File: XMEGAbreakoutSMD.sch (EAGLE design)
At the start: 22 parts, among them IC1 XMEGA16A4A

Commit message: smd breakout finished
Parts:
- added JUMPER1, JUMPER2: 0, fab:RES-US1206FAB
- IC1: value XMEGA16A4A -> XMEGA16A4; device atmel:XMEGA16A4A -> atmel:XMEGA16A4
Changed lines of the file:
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@@
 </classes>
 <parts>
-<part name="IC1" library="atmel" deviceset="XMEGA16A4" device="A"/>
+<part name="IC1" library="atmel" deviceset="XMEGA16A4" device="" value="XMEGA16A4"/>
 <part name="JP2" library="SparkFun" deviceset="M08" device="SMD-STRAIGHT-ALT"/>
 <part name="JP3" library="SparkFun" deviceset="M08" device="SMD-STRAIGHT-ALT"/>
@@
 <part name="D4" library="fab" deviceset="ZENER_DIODE" device="SOD123"/>
 <part name="D5" library="fab" deviceset="ZENER_DIODE" device="SOD123"/>
+<part name="JUMPER1" library="fab" deviceset="RES-US" device="1206FAB" value="0"/>
+<part name="JUMPER2" library="fab" deviceset="RES-US" device="1206FAB" value="0"/>
 </parts>
 <sheets>
@@
 <instance part="D4" gate="1" x="-50.8" y="124.46" rot="R90"/>
 <instance part="D5" gate="1" x="-30.48" y="124.46" rot="R90"/>
+<instance part="JUMPER1" gate="G$1" x="0" y="175.26"/>
+<instance part="JUMPER2" gate="G$1" x="0" y="167.64"/>
 </instances>
 <busses>
@@
 <net name="D+" class="0">
 <segment>
-<pinref part="U$1" gate="G$1" pin="D+"/>
-<wire x1="-60.96" y1="152.4" x2="-55.88" y2="152.4" width="0.1524" layer="91"/>
-<wire x1="-55.88" y1="152.4" x2="-55.88" y2="129.54" width="0.1524" layer="91"/>
-<wire x1="-55.88" y1="129.54" x2="-38.1" y2="129.54" width="0.1524" layer="91"/>
-<label x="-17.78" y="129.54" size="1.778" layer="95"/>
-<pinref part="D2" gate="1" pin="ANODE"/>
-<wire x1="-38.1" y1="129.54" x2="-15.24" y2="129.54" width="0.1524" layer="91"/>
-<wire x1="-38.1" y1="132.08" x2="-38.1" y2="129.54" width="0.1524" layer="91"/>
-<junction x="-38.1" y="129.54"/>
-<pinref part="D3" gate="1" pin="CATHODE"/>
-<wire x1="-38.1" y1="127" x2="-38.1" y2="129.54" width="0.1524" layer="91"/>
-</segment>
-<segment>
 <pinref part="IC1" gate="G$1" pin="PD6"/>
 <pinref part="JP3" gate="G$1" pin="2"/>
@@
 <label x="76.2" y="22.86" size="1.778" layer="95"/>
 </segment>
-</net>
+<segment>
+<pinref part="U$1" gate="G$1" pin="D+"/>
+<wire x1="-60.96" y1="152.4" x2="-55.88" y2="152.4" width="0.1524" layer="91"/>
+<wire x1="-55.88" y1="152.4" x2="-55.88" y2="129.54" width="0.1524" layer="91"/>
+<wire x1="-55.88" y1="129.54" x2="-48.26" y2="129.54" width="0.1524" layer="91"/>
+<wire x1="-38.1" y1="129.54" x2="-15.24" y2="129.54" width="0.1524" layer="91"/>
+<label x="-20.32" y="129.54" size="1.778" layer="95"/>
+<pinref part="D3" gate="1" pin="CATHODE"/>
+<wire x1="-38.1" y1="127" x2="-38.1" y2="129.54" width="0.1524" layer="91"/>
+<junction x="-38.1" y="129.54"/>
+<pinref part="D2" gate="1" pin="ANODE"/>
+<wire x1="-38.1" y1="129.54" x2="-38.1" y2="132.08" width="0.1524" layer="91"/>
+<wire x1="-48.26" y1="129.54" x2="-38.1" y2="129.54" width="0.1524" layer="91"/>
+</segment>
+</net>

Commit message: small changes
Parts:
- added C5: 4.7uF, fab:CAP-US1206
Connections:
- net GND: now also C5.2
- net VBUS: now also C5.1
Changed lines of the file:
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@@
 <part name="JUMPER1" library="fab" deviceset="RES-US" device="1206FAB" value="0"/>
 <part name="JUMPER2" library="fab" deviceset="RES-US" device="1206FAB" value="0"/>
+<part name="C5" library="fab" deviceset="CAP-US" device="1206" value="4.7uF"/>
 </parts>
 <sheets>
@@
 <instance part="JUMPER1" gate="G$1" x="0" y="175.26"/>
 <instance part="JUMPER2" gate="G$1" x="0" y="167.64"/>
+<instance part="C5" gate="G$1" x="33.02" y="160.02" rot="R270"/>
 </instances>
 <busses>
@@
 <wire x1="53.34" y1="170.18" x2="43.18" y2="170.18" width="0.1524" layer="91"/>
 <wire x1="43.18" y1="170.18" x2="43.18" y2="167.64" width="0.1524" layer="91"/>
-<wire x1="43.18" y1="170.18" x2="27.94" y2="170.18" width="0.1524" layer="91"/>
+<wire x1="43.18" y1="170.18" x2="33.02" y2="170.18" width="0.1524" layer="91"/>
 <junction x="43.18" y="170.18"/>
 <label x="27.94" y="170.18" size="1.778" layer="95"/>
+<pinref part="C5" gate="G$1" pin="1"/>
+<wire x1="33.02" y1="170.18" x2="27.94" y2="170.18" width="0.1524" layer="91"/>
+<wire x1="33.02" y1="170.18" x2="33.02" y2="162.56" width="0.1524" layer="91"/>
+<junction x="33.02" y="170.18"/>
 </segment>
 <segment>
@@
 <wire x1="106.68" y1="147.32" x2="106.68" y2="144.78" width="0.1524" layer="91"/>
 <junction x="96.52" y="147.32"/>
-</segment>
-</net>
+<pinref part="C5" gate="G$1" pin="2"/>
+<wire x1="33.02" y1="154.94" x2="33.02" y2="147.32" width="0.1524" layer="91"/>
+<wire x1="33.02" y1="147.32" x2="43.18" y2="147.32" width="0.1524" layer="91"/>
+<junction x="43.18" y="147.32"/>
+</segment>
+</net>

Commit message: final
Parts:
- removed D1, D2, D3, D4, D5: (no value), fab:ZENER_DIODESOD123
- added U$2: INVERTER, SparkFun:INVERTER
- JP1: device SparkFun:M08 -> SparkFun:M081X08_2X1X4A
- JP2, JP3, JP5: device SparkFun:M08SMD-STRAIGHT-ALT -> SparkFun:M081X08
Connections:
- net D+: now also U$2.GND; no longer D2.ANODE, D3.CATHODE
- net D-: now also U$2.Y; no longer D1.ANODE, D4.CATHODE
- net GND: now also U$2.A
- net N$25: no longer D3.ANODE, D4.ANODE, D5.ANODE
- net VBUS: now also U$2.VCC; no longer D1.CATHODE, D2.CATHODE, D5.CATHODE
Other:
- moved on the sheet: C5
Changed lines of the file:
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@@
 <parts>
 <part name="IC1" library="atmel" deviceset="XMEGA16A4" device="" value="XMEGA16A4"/>
-<part name="JP2" library="SparkFun" deviceset="M08" device="SMD-STRAIGHT-ALT"/>
-<part name="JP3" library="SparkFun" deviceset="M08" device="SMD-STRAIGHT-ALT"/>
+<part name="JP2" library="SparkFun" deviceset="M08" device="1X08"/>
+<part name="JP3" library="SparkFun" deviceset="M08" device="1X08"/>
 <part name="C1" library="fab" deviceset="CAP-US" device="1206" value="0.1uF"/>
 <part name="C2" library="fab" deviceset="CAP-US" device="1206" value="10uF"/>
@@
 <part name="GND2" library="SparkFun" deviceset="GND" device=""/>
 <part name="GND3" library="SparkFun" deviceset="GND" device=""/>
-<part name="JP5" library="SparkFun" deviceset="M08" device="SMD-STRAIGHT-ALT"/>
-<part name="JP1" library="SparkFun" deviceset="M08" device=""/>
+<part name="JP5" library="SparkFun" deviceset="M08" device="1X08"/>
+<part name="JP1" library="SparkFun" deviceset="M08" device="1X08_2X1X4A"/>
 <part name="GND4" library="SparkFun" deviceset="GND" device=""/>
 <part name="P+3" library="SparkFun" deviceset="VCC" device=""/>
 <part name="P+4" library="SparkFun" deviceset="VCC" device=""/>
 <part name="GND5" library="SparkFun" deviceset="GND" device=""/>
-<part name="D1" library="fab" deviceset="ZENER_DIODE" device="SOD123"/>
-<part name="D2" library="fab" deviceset="ZENER_DIODE" device="SOD123"/>
-<part name="D3" library="fab" deviceset="ZENER_DIODE" device="SOD123"/>
-<part name="D4" library="fab" deviceset="ZENER_DIODE" device="SOD123"/>
-<part name="D5" library="fab" deviceset="ZENER_DIODE" device="SOD123"/>
 <part name="JUMPER1" library="fab" deviceset="RES-US" device="1206FAB" value="0"/>
 <part name="JUMPER2" library="fab" deviceset="RES-US" device="1206FAB" value="0"/>
 <part name="C5" library="fab" deviceset="CAP-US" device="1206" value="4.7uF"/>
+<part name="U$2" library="SparkFun" deviceset="INVERTER" device=""/>
 </parts>
 <sheets>
@@
 <instance part="P+4" gate="1" x="104.14" y="175.26"/>
 <instance part="GND5" gate="1" x="106.68" y="142.24"/>
-<instance part="D1" gate="1" x="-45.72" y="139.7" rot="R270"/>
-<instance part="D2" gate="1" x="-38.1" y="134.62" rot="R90"/>
-<instance part="D3" gate="1" x="-38.1" y="124.46" rot="R90"/>
-<instance part="D4" gate="1" x="-50.8" y="124.46" rot="R90"/>
-<instance part="D5" gate="1" x="-30.48" y="124.46" rot="R90"/>
 <instance part="JUMPER1" gate="G$1" x="0" y="175.26"/>
 <instance part="JUMPER2" gate="G$1" x="0" y="167.64"/>
-<instance part="C5" gate="G$1" x="33.02" y="160.02" rot="R270"/>
+<instance part="C5" gate="G$1" x="30.48" y="162.56" rot="R270"/>
+<instance part="U$2" gate="G$1" x="30.48" y="116.84"/>
 </instances>
 <busses>
@@
 <wire x1="53.34" y1="170.18" x2="43.18" y2="170.18" width="0.1524" layer="91"/>
 <wire x1="43.18" y1="170.18" x2="43.18" y2="167.64" width="0.1524" layer="91"/>
-<wire x1="43.18" y1="170.18" x2="33.02" y2="170.18" width="0.1524" layer="91"/>
+<wire x1="43.18" y1="170.18" x2="30.48" y2="170.18" width="0.1524" layer="91"/>
 <junction x="43.18" y="170.18"/>
 <label x="27.94" y="170.18" size="1.778" layer="95"/>
 <pinref part="C5" gate="G$1" pin="1"/>
-<wire x1="33.02" y1="170.18" x2="27.94" y2="170.18" width="0.1524" layer="91"/>
-<wire x1="33.02" y1="170.18" x2="33.02" y2="162.56" width="0.1524" layer="91"/>
-<junction x="33.02" y="170.18"/>
-</segment>
-<segment>
-<wire x1="-45.72" y1="137.16" x2="-40.64" y2="137.16" width="0.1524" layer="91"/>
-<wire x1="-40.64" y1="137.16" x2="-38.1" y2="137.16" width="0.1524" layer="91"/>
-<wire x1="-38.1" y1="137.16" x2="-35.56" y2="137.16" width="0.1524" layer="91"/>
-<wire x1="-35.56" y1="137.16" x2="-30.48" y2="137.16" width="0.1524" layer="91"/>
-<label x="-22.86" y="137.16" size="1.778" layer="95"/>
-<pinref part="D1" gate="1" pin="CATHODE"/>
-<pinref part="D2" gate="1" pin="CATHODE"/>
-<junction x="-38.1" y="137.16"/>
-<pinref part="D5" gate="1" pin="CATHODE"/>
-<wire x1="-30.48" y1="137.16" x2="-15.24" y2="137.16" width="0.1524" layer="91"/>
-<wire x1="-30.48" y1="127" x2="-30.48" y2="137.16" width="0.1524" layer="91"/>
-<junction x="-30.48" y="137.16"/>
+<wire x1="30.48" y1="170.18" x2="27.94" y2="170.18" width="0.1524" layer="91"/>
+<wire x1="30.48" y1="165.1" x2="30.48" y2="170.18" width="0.1524" layer="91"/>
+<junction x="30.48" y="170.18"/>
+</segment>
+<segment>
+<pinref part="U$2" gate="G$1" pin="VCC"/>
+<wire x1="40.64" y1="121.92" x2="50.8" y2="121.92" width="0.1524" layer="91"/>
+<label x="45.72" y="121.92" size="1.778" layer="95"/>
 </segment>
 </net>
@@
 <wire x1="-55.88" y1="152.4" x2="-55.88" y2="129.54" width="0.1524" layer="91"/>
 <wire x1="-55.88" y1="129.54" x2="-48.26" y2="129.54" width="0.1524" layer="91"/>
-<wire x1="-38.1" y1="129.54" x2="-15.24" y2="129.54" width="0.1524" layer="91"/>
-<label x="-20.32" y="129.54" size="1.778" layer="95"/>
-<pinref part="D3" gate="1" pin="CATHODE"/>
-<wire x1="-38.1" y1="127" x2="-38.1" y2="129.54" width="0.1524" layer="91"/>
-<junction x="-38.1" y="129.54"/>
-<pinref part="D2" gate="1" pin="ANODE"/>
-<wire x1="-38.1" y1="129.54" x2="-38.1" y2="132.08" width="0.1524" layer="91"/>
+<label x="-40.64" y="129.54" size="1.778" layer="95"/>
 <wire x1="-48.26" y1="129.54" x2="-38.1" y2="129.54" width="0.1524" layer="91"/>
+</segment>
+<segment>
+<pinref part="U$2" gate="G$1" pin="GND"/>
+<wire x1="20.32" y1="111.76" x2="7.62" y2="111.76" width="0.1524" layer="91"/>
+<label x="7.62" y="111.76" size="1.778" layer="95"/>
 </segment>
 </net>
@@
 <junction x="96.52" y="147.32"/>
 <pinref part="C5" gate="G$1" pin="2"/>
-<wire x1="33.02" y1="154.94" x2="33.02" y2="147.32" width="0.1524" layer="91"/>
-<wire x1="33.02" y1="147.32" x2="43.18" y2="147.32" width="0.1524" layer="91"/>
+<wire x1="30.48" y1="157.48" x2="30.48" y2="147.32" width="0.1524" layer="91"/>
+<wire x1="30.48" y1="147.32" x2="43.18" y2="147.32" width="0.1524" layer="91"/>
 <junction x="43.18" y="147.32"/>
+</segment>
+<segment>
+<pinref part="U$2" gate="G$1" pin="A"/>
+<wire x1="20.32" y1="116.84" x2="7.62" y2="116.84" width="0.1524" layer="91"/>
+<label x="7.62" y="116.84" size="1.778" layer="95"/>
 </segment>
 </net>
@@
 <wire x1="-50.8" y1="154.94" x2="-50.8" y2="144.78" width="0.1524" layer="91"/>
 <wire x1="-50.8" y1="144.78" x2="-45.72" y2="144.78" width="0.1524" layer="91"/>
-<label x="-17.78" y="144.78" size="1.778" layer="95"/>
+<label x="-40.64" y="144.78" size="1.778" layer="95"/>
 <wire x1="-45.72" y1="144.78" x2="-40.64" y2="144.78" width="0.1524" layer="91"/>
 <wire x1="-40.64" y1="144.78" x2="-35.56" y2="144.78" width="0.1524" layer="91"/>
-<wire x1="-35.56" y1="144.78" x2="-15.24" y2="144.78" width="0.1524" layer="91"/>
-<pinref part="D1" gate="1" pin="ANODE"/>
-<wire x1="-45.72" y1="144.78" x2="-45.72" y2="142.24" width="0.1524" layer="91"/>
-<junction x="-45.72" y="144.78"/>
-<pinref part="D4" gate="1" pin="CATHODE"/>
-<wire x1="-50.8" y1="127" x2="-50.8" y2="144.78" width="0.1524" layer="91"/>
-<junction x="-50.8" y="144.78"/>
 </segment>
 <segment>
@@
 <wire x1="73.66" y1="25.4" x2="83.82" y2="25.4" width="0.1524" layer="91"/>
 <label x="76.2" y="25.4" size="1.778" layer="95"/>
+</segment>
+<segment>
+<pinref part="U$2" gate="G$1" pin="Y"/>
+<wire x1="40.64" y1="111.76" x2="50.8" y2="111.76" width="0.1524" layer="91"/>
+<label x="45.72" y="111.76" size="1.778" layer="95"/>
 </segment>
 </net>
@@
 <junction x="-50.8" y="177.8"/>
 <wire x1="-73.66" y1="165.1" x2="-66.04" y2="165.1" width="0.1524" layer="91"/>
-<wire x1="-66.04" y1="147.32" x2="-66.04" y2="119.38" width="0.1524" layer="91"/>
-<wire x1="-66.04" y1="119.38" x2="-50.8" y2="119.38" width="0.1524" layer="91"/>
-<pinref part="D3" gate="1" pin="ANODE"/>
-<wire x1="-50.8" y1="119.38" x2="-38.1" y2="119.38" width="0.1524" layer="91"/>
-<wire x1="-38.1" y1="119.38" x2="-30.48" y2="119.38" width="0.1524" layer="91"/>
-<wire x1="-30.48" y1="119.38" x2="-15.24" y2="119.38" width="0.1524" layer="91"/>
-<wire x1="-38.1" y1="119.38" x2="-38.1" y2="121.92" width="0.1524" layer="91"/>
-<junction x="-38.1" y="119.38"/>
-<pinref part="D4" gate="1" pin="ANODE"/>
-<wire x1="-50.8" y1="119.38" x2="-50.8" y2="121.92" width="0.1524" layer="91"/>
-<junction x="-50.8" y="119.38"/>
-<pinref part="D5" gate="1" pin="ANODE"/>
-<wire x1="-30.48" y1="119.38" x2="-30.48" y2="121.92" width="0.1524" layer="91"/>
-<junction x="-30.48" y="119.38"/>
-</segment>
-</net>
+<wire x1="-66.04" y1="147.32" x2="-66.04" y2="134.62" width="0.1524" layer="91"/>
+</segment>
+</net>

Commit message: reorganizing
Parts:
- JP1: device SparkFun:M081X08_2X1X4A -> SparkFun:M08
- JP2, JP3, JP5: device SparkFun:M081X08 -> SparkFun:M08SMD-STRAIGHT-ALT
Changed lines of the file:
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@@
 <parts>
 <part name="IC1" library="atmel" deviceset="XMEGA16A4" device="" value="XMEGA16A4"/>
-<part name="JP2" library="SparkFun" deviceset="M08" device="1X08"/>
-<part name="JP3" library="SparkFun" deviceset="M08" device="1X08"/>
+<part name="JP2" library="SparkFun" deviceset="M08" device="SMD-STRAIGHT-ALT"/>
+<part name="JP3" library="SparkFun" deviceset="M08" device="SMD-STRAIGHT-ALT"/>
 <part name="C1" library="fab" deviceset="CAP-US" device="1206" value="0.1uF"/>
 <part name="C2" library="fab" deviceset="CAP-US" device="1206" value="10uF"/>
@@
 <part name="GND2" library="SparkFun" deviceset="GND" device=""/>
 <part name="GND3" library="SparkFun" deviceset="GND" device=""/>
-<part name="JP5" library="SparkFun" deviceset="M08" device="1X08"/>
-<part name="JP1" library="SparkFun" deviceset="M08" device="1X08_2X1X4A"/>
+<part name="JP5" library="SparkFun" deviceset="M08" device="SMD-STRAIGHT-ALT"/>
+<part name="JP1" library="SparkFun" deviceset="M08" device=""/>
 <part name="GND4" library="SparkFun" deviceset="GND" device=""/>
 <part name="P+3" library="SparkFun" deviceset="VCC" device=""/>

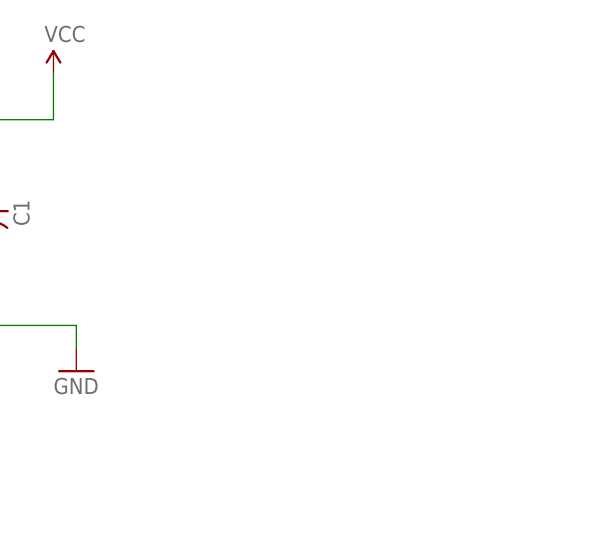
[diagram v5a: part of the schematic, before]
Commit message: power pins broken out
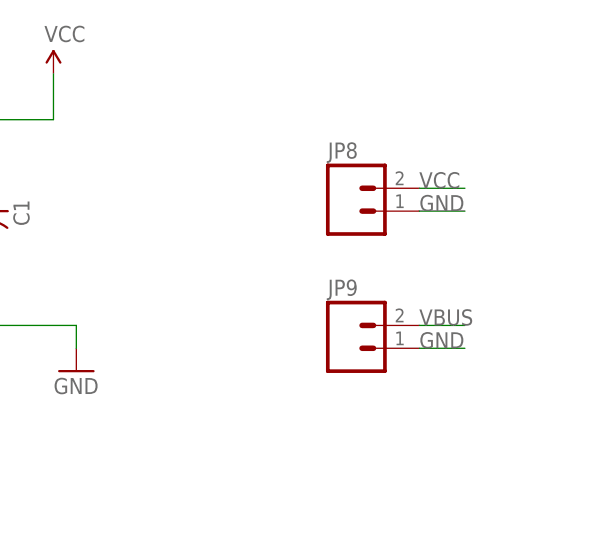
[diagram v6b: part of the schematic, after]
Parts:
- added JP8, JP9: (no value), SparkFun:M02
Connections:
- net GND: now also JP8.1, JP9.1
- net VBUS: now also JP9.2
- net VCC: now also JP8.2
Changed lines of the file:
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@@
 <part name="C5" library="fab" deviceset="CAP-US" device="1206" value="4.7uF"/>
 <part name="U$2" library="SparkFun" deviceset="INVERTER" device=""/>
+<part name="JP8" library="SparkFun" deviceset="M02" device=""/>
+<part name="JP9" library="SparkFun" deviceset="M02" device=""/>
 </parts>
 <sheets>
@@
 <instance part="C5" gate="G$1" x="30.48" y="162.56" rot="R270"/>
 <instance part="U$2" gate="G$1" x="30.48" y="116.84"/>
+<instance part="JP8" gate="G$1" x="137.16" y="160.02"/>
+<instance part="JP9" gate="G$1" x="137.16" y="144.78"/>
 </instances>
 <busses>
@@
 <wire x1="40.64" y1="121.92" x2="50.8" y2="121.92" width="0.1524" layer="91"/>
 <label x="45.72" y="121.92" size="1.778" layer="95"/>
+</segment>
+<segment>
+<pinref part="JP9" gate="G$1" pin="2"/>
+<wire x1="144.78" y1="147.32" x2="149.86" y2="147.32" width="0.1524" layer="91"/>
+<label x="144.78" y="147.32" size="1.778" layer="95"/>
 </segment>
 </net>
@@
 <label x="7.62" y="116.84" size="1.778" layer="95"/>
 </segment>
+<segment>
+<pinref part="JP8" gate="G$1" pin="1"/>
+<wire x1="144.78" y1="160.02" x2="149.86" y2="160.02" width="0.1524" layer="91"/>
+<label x="144.78" y="160.02" size="1.778" layer="95"/>
+</segment>
+<segment>
+<pinref part="JP9" gate="G$1" pin="1"/>
+<wire x1="144.78" y1="144.78" x2="149.86" y2="144.78" width="0.1524" layer="91"/>
+<label x="144.78" y="144.78" size="1.778" layer="95"/>
+</segment>
 </net>
 <net name="VCC" class="0">
@@
 <junction x="96.52" y="170.18"/>
 </segment>
-</net>
+<segment>
+<pinref part="JP8" gate="G$1" pin="2"/>
+<wire x1="144.78" y1="162.56" x2="149.86" y2="162.56" width="0.1524" layer="91"/>
+<label x="144.78" y="162.56" size="1.778" layer="95"/>
+</segment>
+</net>

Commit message: latest
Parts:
- added JP6: (no value), fab:PINHD-2X3-SMD
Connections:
- new net DAT: IC1.PDI_DATA, JP6.1
- net GND: now also JP6.6
- net RESET: now also JP6.5; no longer JP4.5
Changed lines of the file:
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@@
 <part name="JP8" library="SparkFun" deviceset="M02" device=""/>
 <part name="JP9" library="SparkFun" deviceset="M02" device=""/>
+<part name="JP6" library="fab" deviceset="PINHD-2X3-SMD" device=""/>
+<part name="GND6" library="SparkFun" deviceset="GND" device=""/>
 </parts>
 <sheets>
@@
 <instance part="JP8" gate="G$1" x="137.16" y="160.02"/>
 <instance part="JP9" gate="G$1" x="137.16" y="144.78"/>
+<instance part="JP6" gate="A" x="139.7" y="20.32"/>
+<instance part="GND6" gate="1" x="157.48" y="12.7"/>
 </instances>
 <busses>
@@
 </segment>
 <segment>
-<pinref part="JP4" gate="A" pin="5"/>
-<wire x1="137.16" y1="45.72" x2="121.92" y2="45.72" width="0.1524" layer="91"/>
-<label x="121.92" y="45.72" size="1.778" layer="95"/>
+<pinref part="JP6" gate="A" pin="5"/>
+<wire x1="137.16" y1="17.78" x2="121.92" y2="17.78" width="0.1524" layer="91"/>
+<label x="121.92" y="17.78" size="1.778" layer="95"/>
 </segment>
 </net>
@@
 <label x="144.78" y="144.78" size="1.778" layer="95"/>
 </segment>
+<segment>
+<pinref part="JP6" gate="A" pin="6"/>
+<wire x1="144.78" y1="17.78" x2="157.48" y2="17.78" width="0.1524" layer="91"/>
+<pinref part="GND6" gate="1" pin="GND"/>
+<wire x1="157.48" y1="17.78" x2="157.48" y2="15.24" width="0.1524" layer="91"/>
+</segment>
 </net>
 <net name="VCC" class="0">
@@
 </segment>
 </net>
+<net name="DAT" class="0">
+<segment>
+<pinref part="JP6" gate="A" pin="1"/>
+<wire x1="137.16" y1="22.86" x2="121.92" y2="22.86" width="0.1524" layer="91"/>
+<label x="121.92" y="22.86" size="1.778" layer="95"/>
+</segment>
+<segment>
+<pinref part="IC1" gate="G$1" pin="PDI_DATA"/>
+<wire x1="20.32" y1="78.74" x2="7.62" y2="78.74" width="0.1524" layer="91"/>
+<label x="7.62" y="78.74" size="1.778" layer="95"/>
+</segment>
+</net>
